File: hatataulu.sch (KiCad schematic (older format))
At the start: 16 parts

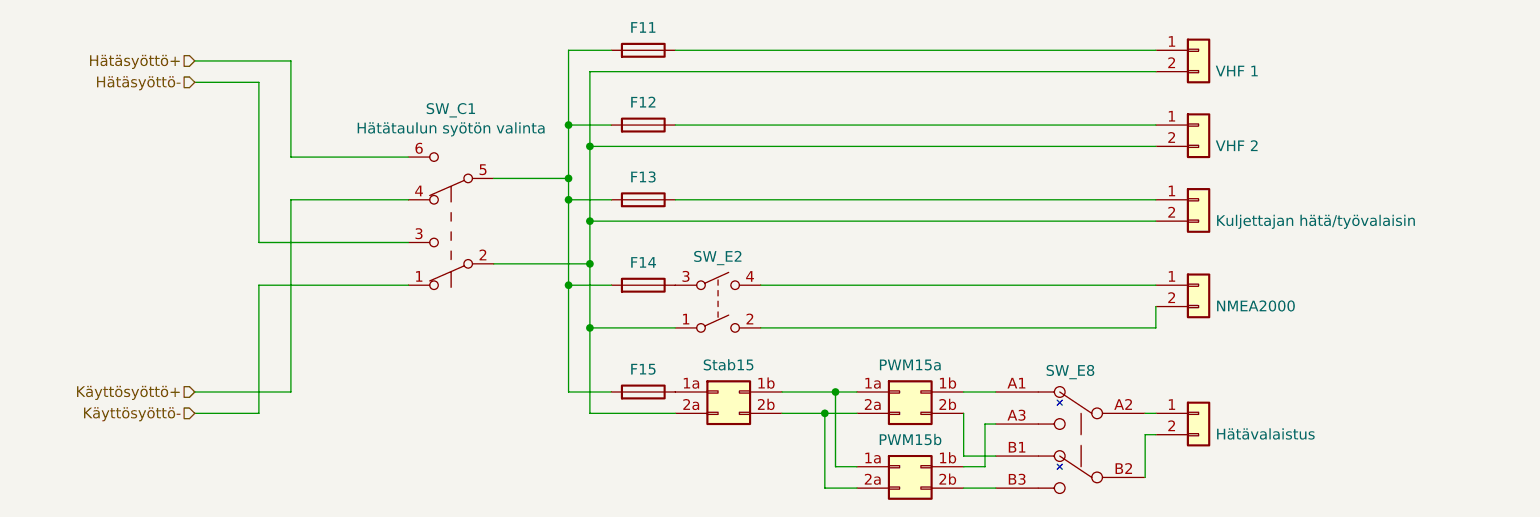
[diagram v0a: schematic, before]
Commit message: IDitä muutettu osoitteistusluonnoksen mukaan
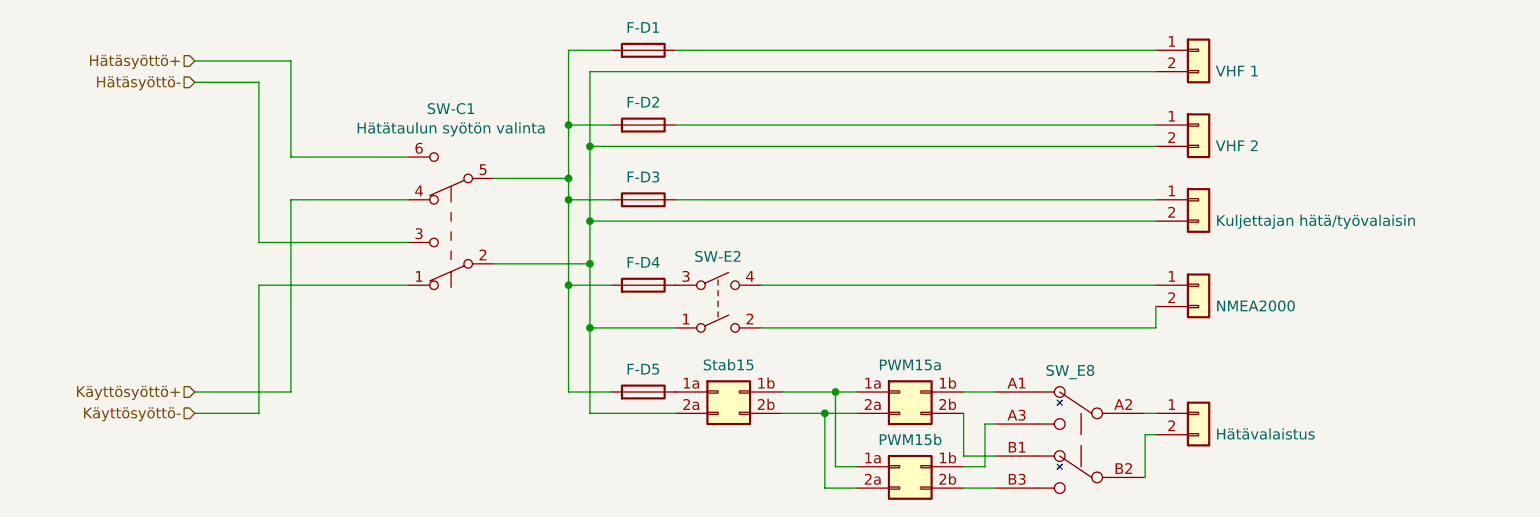
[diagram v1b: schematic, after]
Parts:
- renumbered F11 to F-D1, F12 to F-D2, F13 to F-D3, F14 to F-D4, F15 to F-D5, SW_C1 to SW-C1, SW_E2 to SW-E2
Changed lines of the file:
@@
 Käyttösyöttö-
 $Comp
-L Switch:SW_Push_DPDT SW_C1
+L Switch:SW_Push_DPDT SW-C1
 U 1 1 5DE4DBD8
 P 2400 1600
-F 0 "SW_C1" H 2400 1075 50  0000 C CNN
+F 0 "SW-C1" H 2400 1075 50  0000 C CNN
 F 1 "Hätätaulun syötön valinta" H 2400 1166 50  0000 C CNN
 F 2 "" H 2400 1800 50  0001 C CNN
@@
 $EndComp
 $Comp
-L Device:Fuse F11
+L Device:Fuse F-D1
 U 1 1 5DE528DF
 P 3300 800
-F 0 "F11" V 3405 800 50  0000 C CNN
+F 0 "F-D1" V 3405 800 50  0000 C CNN
 F 1 "Fuse" V 3406 800 50  0001 C CNN
 F 2 "" V 3230 800 50  0001 C CNN
@@
 $EndComp
 $Comp
-L Device:Fuse F13
+L Device:Fuse F-D3
 U 1 1 5DE6A334
 P 3300 1500
-F 0 "F13" V 3405 1500 50  0000 C CNN
+F 0 "F-D3" V 3405 1500 50  0000 C CNN
 F 1 "Fuse" V 3406 1500 50  0001 C CNN
 F 2 "" V 3230 1500 50  0001 C CNN
@@
 $EndComp
 $Comp
-L Device:Fuse F14
+L Device:Fuse F-D4
 U 1 1 5DE6C7A1
 P 3300 1900
-F 0 "F14" V 3405 1900 50  0000 C CNN
+F 0 "F-D4" V 3405 1900 50  0000 C CNN
 F 1 "Fuse" V 3406 1900 50  0001 C CNN
 F 2 "" V 3230 1900 50  0001 C CNN
@@
 $EndComp
 $Comp
-L Device:Fuse F12
+L Device:Fuse F-D2
 U 1 1 5DE691F3
 P 3300 1150
-F 0 "F12" V 3405 1150 50  0000 C CNN
+F 0 "F-D2" V 3405 1150 50  0000 C CNN
 F 1 "Fuse" V 3406 1150 50  0001 C CNN
 F 2 "" V 3230 1150 50  0001 C CNN
@@
 $EndComp
 $Comp
-L Device:Fuse F15
+L Device:Fuse F-D5
 U 1 1 5DF144C1
 P 3300 2400
-F 0 "F15" V 3405 2400 50  0000 C CNN
+F 0 "F-D5" V 3405 2400 50  0000 C CNN
 F 1 "Fuse" V 3406 2400 50  0001 C CNN
 F 2 "" V 3230 2400 50  0001 C CNN
@@
 	5650 2600 5650 2800
 $Comp
-L Switch:SW_DPST SW_E2
+L Switch:SW_DPST SW-E2
 U 1 1 5E02B31D
 P 3650 2000
-F 0 "SW_E2" H 3650 2233 50  0000 C CNN
+F 0 "SW-E2" H 3650 2233 50  0000 C CNN
 F 1 "SW_DPST" H 3650 2234 50  0001 C CNN
 F 2 "" H 3650 2000 50  0001 C CNN
